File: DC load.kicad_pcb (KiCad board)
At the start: 2 copper layers, 33.3 x 44.4 mm, 23 parts, among them J1 CTL IN, J2 CTL OUT, J3 B+, J4 B-, Q1 IRFI540, U1 LM324

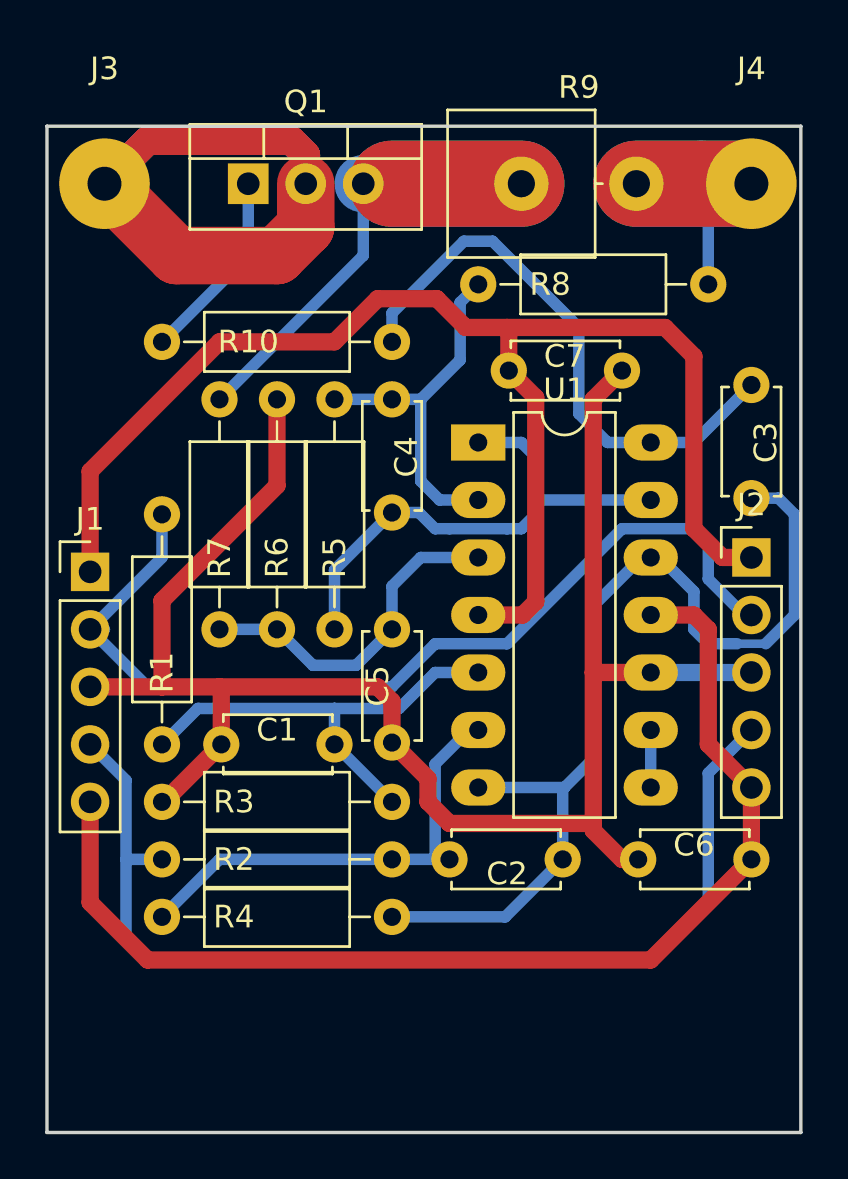
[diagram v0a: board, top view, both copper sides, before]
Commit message: Diagram: * Small offset so 0V is guaranteed to shut current off * Added zener to avoid high voltages and polarity reversal PCB: * Layout updated to new schematics
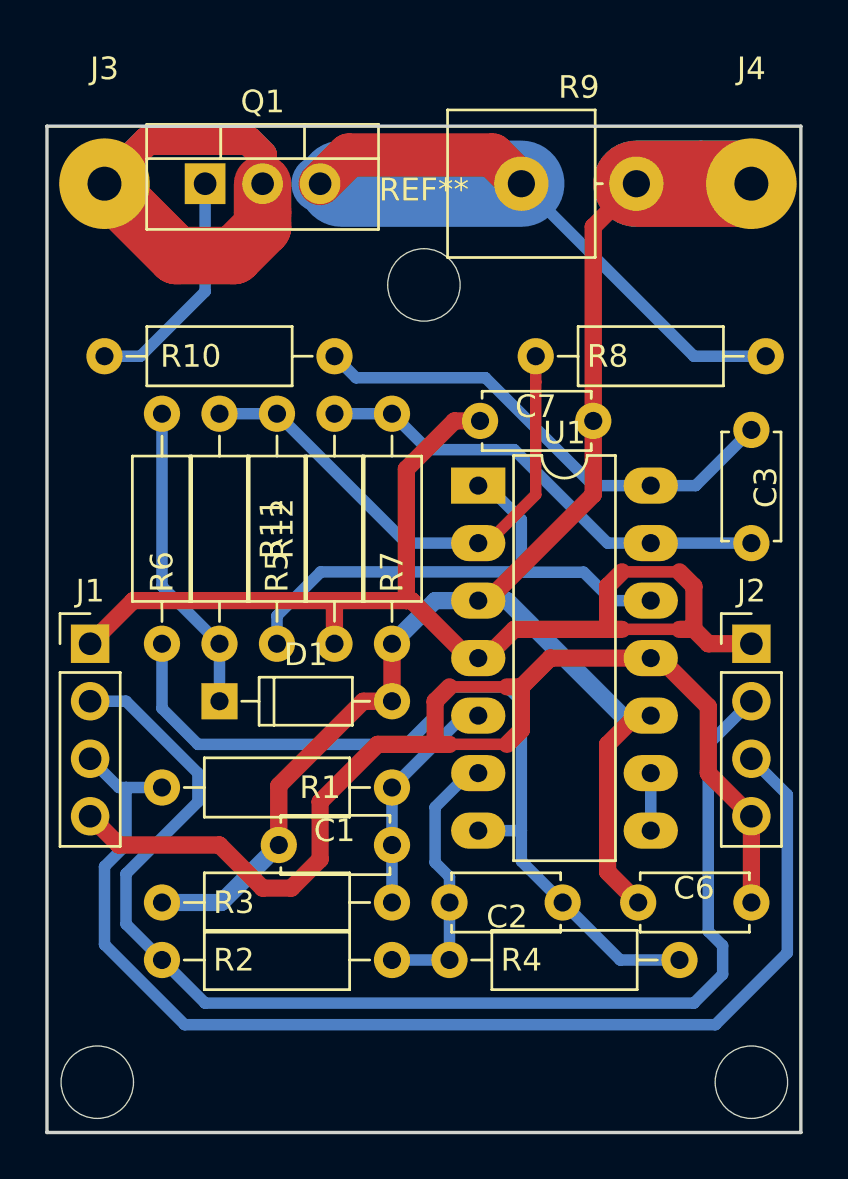
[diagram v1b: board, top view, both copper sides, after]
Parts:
- removed C4, C5: 1n, Capacitors_THT:C_Disc_D4.7mm_W2.5mm_P5.00mm
- added D1: 2v7, Diodes_THT:D_DO-35_SOD27_P7.62mm_Horizontal, F.Cu at (134.6, 120.7)
- added M1: MountingHole_3.2mm_M3, Mounting_Holes:MountingHole_3.2mm_M3, F.Cu at (129.2, 137.5)
- added M2: MountingHole_3.2mm_M3, Mounting_Holes:MountingHole_3.2mm_M3, F.Cu at (158.1, 137.5)
- added R11: 3k01, Resistors_THT:R_Axial_DIN0207_L6.3mm_D2.5mm_P10.16mm_Horizontal, F.Cu at (134.6, 108.0)
- added R12: 2M37, Resistors_THT:R_Axial_DIN0207_L6.3mm_D2.5mm_P10.16mm_Horizontal, F.Cu at (139.7, 118.1)
- added REF**: MountingHole_3.2mm_M3, Mounting_Holes:MountingHole_3.2mm_M3, F.Cu at (143.7, 102.3)
- C3: value 1n -> 10n
- J1, J2: footprint Pin_Headers:Pin_Header_Straight_1x05_Pitch2.54mm -> Pin_Headers:Pin_Header_Straight_1x04_Pitch2.54mm
- R3, R4: value 10k -> 5k11
- R5: value 13k3 -> 12k1
- R6: value 13k3 -> 3k01
- R7: value 1k -> 10k
- moved R4 12.8 mm to (154.9, 132.1)
- moved R1 10.3 mm to (142.2, 124.5), turned to 180 degrees
- moved R7 7.65 mm to (142.2, 108.0)
- moved C1 5.12 mm to (137.2, 127.0)
- moved R6 5.12 mm to (132.1, 118.1)
- moved R2 4.45 mm to (142.2, 132.1)
- moved R3 4.44 mm to (142.2, 129.5)
- moved R8 4.07 mm to (158.8, 105.4)
- moved J2 3.81 mm to (158.1, 118.1)
- moved J1 3.17 mm to (128.9, 118.1)
- moved R10 2.62 mm to (129.5, 105.4)
- moved R5 2.62 mm to (137.2, 108.0)
- moved C7 2.56 mm to (146.1, 108.3)
- moved C3 1.98 mm to (158.1, 108.7)
- moved U1 1.91 mm to (146.1, 111.1)
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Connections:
- C3 pad 2: Net-(C2-Pad1) -> Net-(C3-Pad2)
- J1 pad 3: GND -> Net-(J1-Pad3)
- J1 pad 4: Net-(J1-Pad4) -> VSS
- J2 pad 3: GND -> Net-(J1-Pad3)
- J2 pad 4: Net-(J1-Pad4) -> VSS
- J4 pad 1: Net-(J4-Pad1) -> GND
- R1 pad 2: Net-(J1-Pad2) -> Net-(J1-Pad3)
- R2 pad 2: Net-(J1-Pad4) -> Net-(J1-Pad2)
- R5 pad 2: Net-(C4-Pad2) -> Net-(R5-Pad2)
- R6 pad 1: Net-(C5-Pad1) -> Net-(C2-Pad1)
- R6 pad 2: GND -> Net-(D1-Pad1)
- R7 pad 1: Net-(Q1-Pad3) -> Net-(C3-Pad2)
- R7 pad 2: Net-(C5-Pad1) -> GND
- R8 pad 1: Net-(J4-Pad1) -> Net-(Q1-Pad3)
- R9 pad 2: Net-(J4-Pad1) -> GND
- U1 pad 1: Net-(C4-Pad2) -> Net-(R5-Pad2)
- U1 pad 12: Net-(C2-Pad1) -> Net-(R5-Pad2)
- U1 pad 13: Net-(C4-Pad2) -> Net-(C3-Pad2)
- U1 pad 3: Net-(C5-Pad1) -> GND
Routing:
- net Net-(J1-Pad3): track 0.00 -> 53.2 mm
- net Net-(J1-Pad4): track 46.4 -> 0.00 mm
- net Net-(R5-Pad2): track 0.00 -> 24.3 mm
- net Net-(C4-Pad2): track 23.5 -> 0.00 mm
- net Net-(C3-Pad2): track 0.00 -> 20.8 mm
- net Net-(C5-Pad1): track 15.2 -> 0.00 mm
- net Net-(J4-Pad1): track 14.7 -> 0.00 mm
- net Net-(D1-Pad1): track 0.00 -> 13.8 mm
- net Net-(J1-Pad2): track 42.7 -> 55.5 mm
- net Net-(C1-Pad2): track 20.5 -> 10.2 mm
- net VDD: track 61.4 -> 51.8 mm
- net Net-(Q1-Pad3): track 26.1 -> 35.0 mm
- net Net-(C2-Pad2): track 20.5 -> 12.1 mm
- net Net-(R11-Pad1): track 16.4 -> 23.3 mm
- net Net-(J3-Pad1): track 35.1 -> 29.3 mm
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
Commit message: Version 0.3: Reverted to more conventional opamp usage
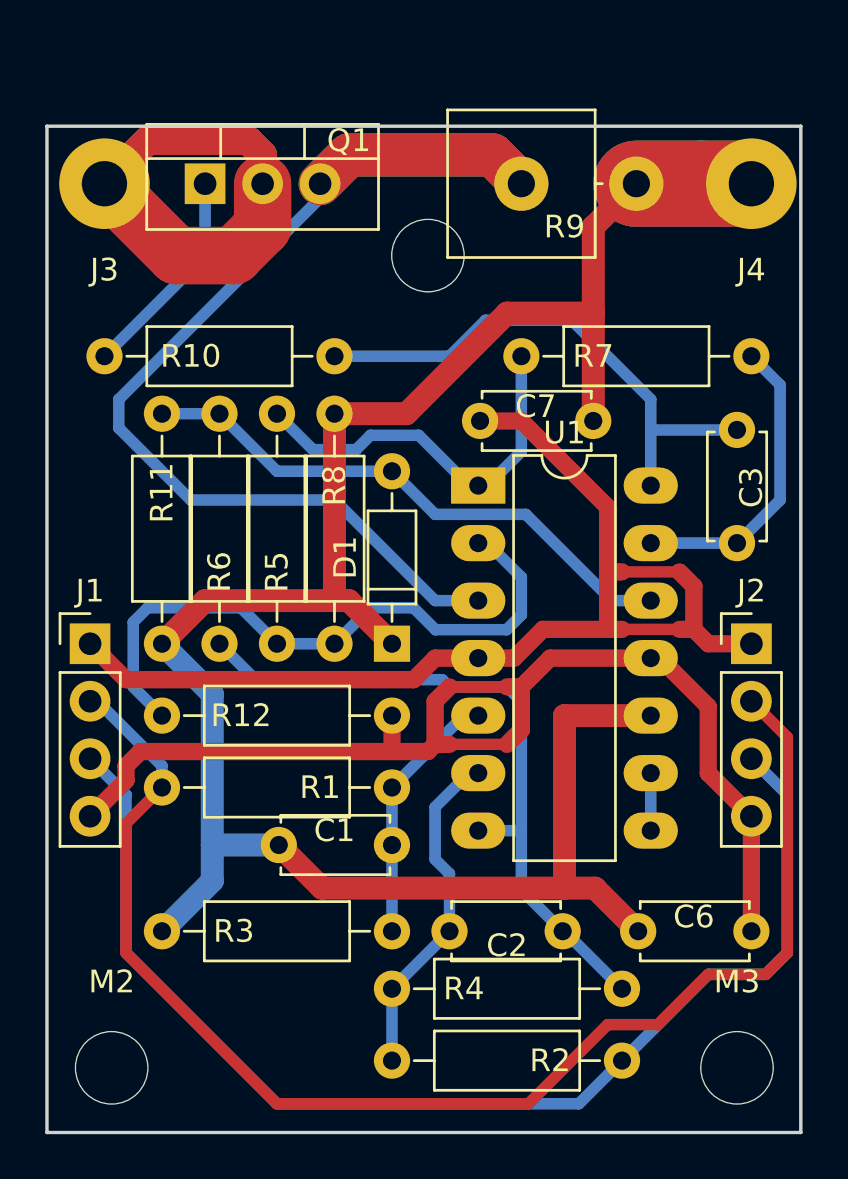
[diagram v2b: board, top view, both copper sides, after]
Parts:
- removed M1, REF**: MountingHole_3.2mm_M3, Mounting_Holes:MountingHole_3.2mm_M3
- added M3: 3.2mm, Mounting_Holes:MountingHole_3.2mm_M3_DIN965, F.Cu at (157.5, 136.8)
- added MP1: 3.2mm, Mounting_Holes:MountingHole_3.2mm_M3_DIN965, F.Cu at (143.8, 101.0)
- C3: value 10n -> 22n
- M2: value MountingHole_3.2mm_M3 -> 3.2mm; footprint Mounting_Holes:MountingHole_3.2mm_M3 -> Mounting_Holes:MountingHole_3.2mm_M3_DIN965
- R11, R6: value 3k01 -> 20k
- R12: value 2M37 -> 2M2
- R3, R4: value 5k11 -> 2k49
- R5: value 12k1 -> 2k
- moved M2 28.3 mm to (129.9, 136.8)
- moved R8 22.9 mm to (139.7, 118.1), turned to 90 degrees
- moved R7 16.1 mm to (158.1, 105.4), turned to 180 degrees
- moved R11 10.5 mm to (132.1, 118.1), turned to 90 degrees
- moved R12 8.25 mm to (132.1, 121.3), turned to 0 degrees
- moved D1 8.03 mm to (142.2, 118.1), turned to 90 degrees
- moved R2 4.44 mm to (142.2, 136.5), turned to 0 degrees
- moved R4 2.84 mm to (152.4, 133.3)
- moved R6 2.54 mm to (134.6, 118.1)
- moved C2 1.27 mm to (149.8, 130.8)
- moved C6 1.27 mm to (158.1, 130.8)
- moved R3 1.27 mm to (142.2, 130.8)
- moved C3 0.64 mm to (157.5, 108.7)
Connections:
- D1 pad 1: Net-(D1-Pad1) -> GND
- D1 pad 2: GND -> Net-(D1-Pad2)
- R1 pad 2: Net-(J1-Pad3) -> Net-(J1-Pad2)
- R11 pad 1: Net-(R11-Pad1) -> GND
- R11 pad 2: Net-(D1-Pad1) -> Net-(D1-Pad2)
- R12 pad 1: VDD -> Net-(R12-Pad1)
- R12 pad 2: Net-(C3-Pad2) -> VSS
- R2 pad 2: Net-(J1-Pad2) -> Net-(J1-Pad3)
- R5 pad 1: Net-(R11-Pad1) -> Net-(R5-Pad1)
- R5 pad 2: Net-(R5-Pad2) -> Net-(R12-Pad1)
- R6 pad 2: Net-(D1-Pad1) -> Net-(D1-Pad2)
- R7 pad 2: GND -> Net-(R5-Pad1)
- R8 pad 1: Net-(Q1-Pad3) -> Net-(R12-Pad1)
- R8 pad 2: Net-(R11-Pad1) -> GND
- U1 pad 1: Net-(R5-Pad2) -> Net-(R5-Pad1)
- U1 pad 12: Net-(R5-Pad2) -> Net-(D1-Pad2)
- U1 pad 2: Net-(R11-Pad1) -> Net-(R12-Pad1)
- U1 pad 3: GND -> Net-(Q1-Pad3)
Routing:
- net Net-(R12-Pad1): track 0.00 -> 28.6 mm
- net GND: track 74.4 -> 101.6 mm
- net Net-(D1-Pad2): track 0.00 -> 25.4 mm
- net Net-(R5-Pad2): track 24.3 -> 0.00 mm
- net Net-(R11-Pad1): track 23.3 -> 0.00 mm
- net Net-(Q1-Pad3): track 35.0 -> 53.8 mm
- net Net-(R5-Pad1): track 0.00 -> 17.5 mm
- net Net-(D1-Pad1): track 13.8 -> 0.00 mm
- net Net-(C2-Pad1): track 38.8 -> 30.9 mm
- net Net-(C3-Pad2): track 20.8 -> 13.4 mm
- net Net-(J1-Pad2): track 55.5 -> 59.8 mm
- net Net-(C2-Pad2): track 12.1 -> 15.0 mm
- net VDD: track 51.8 -> 49.6 mm
- net Net-(C3-Pad1): track 21.8 -> 23.7 mm
- net Net-(C1-Pad2): track 10.2 -> 11.5 mm
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
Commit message: Prepare for production
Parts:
- R9: footprint Resistors_THT:R_Axial_Power_L20.0mm_W6.4mm_P5.08mm_Vertical -> Capacitors_THT:C_Rect_L7.2mm_W4.5mm_P5.00mm_FKS2_FKP2_MKS2_MKP2
- moved D1 116.7 mm to (48.6, 48.6), turned to 270 degrees
- moved Q1 112.3 mm to (40.3, 35.9)
- moved R11 112.3 mm to (38.4, 56.2)
- moved R9 112.3 mm to (54.3, 35.9)
- moved B- 112.3 mm to (64.5, 35.9)
- moved C1 112.3 mm to (43.6, 65.1)
- moved C6 112.3 mm to (64.5, 68.9)
- moved J2 112.3 mm to (64.5, 56.2)
- moved R1 112.3 mm to (48.6, 62.5)
- moved R12 112.3 mm to (38.4, 59.4)
- moved R2 112.3 mm to (48.6, 74.6)
- moved R3 112.3 mm to (48.6, 68.9)
- moved R4 112.3 mm to (58.7, 71.4)
- moved R7 112.3 mm to (64.5, 43.5)
- moved U1 112.3 mm to (52.4, 49.2)
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- renumbered J3 to B+, J4 to B-, MP1 to M1
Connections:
- D1 pad 1: GND -> Net-(D1-Pad1)
- D1 pad 2: Net-(D1-Pad2) -> GND
- R11 pad 2: Net-(D1-Pad2) -> Net-(D1-Pad1)
- R6 pad 2: Net-(D1-Pad2) -> Net-(D1-Pad1)
- U1 pad 12: Net-(D1-Pad2) -> Net-(D1-Pad1)
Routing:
- net Net-(D1-Pad1): track 0.00 -> 25.4 mm
- net Net-(D1-Pad2): track 25.4 -> 0.00 mm
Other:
- board size 33.3 x 44.4 mm -> 100 x 88.9 mm
- board text added: "DC LOAD"
- board text added: "FEF 2019"
- board text added: "v1.0"

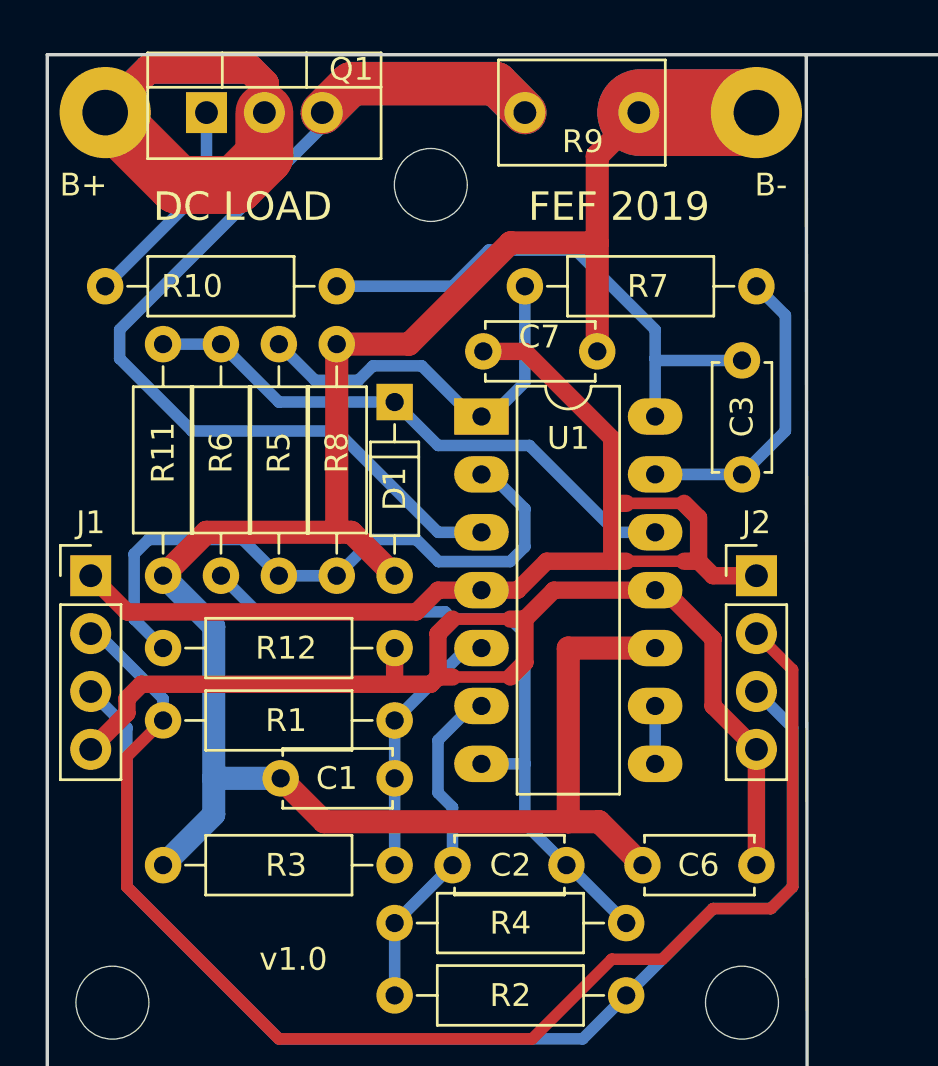
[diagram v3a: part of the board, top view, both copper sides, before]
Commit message: Changed overcurrent limiter
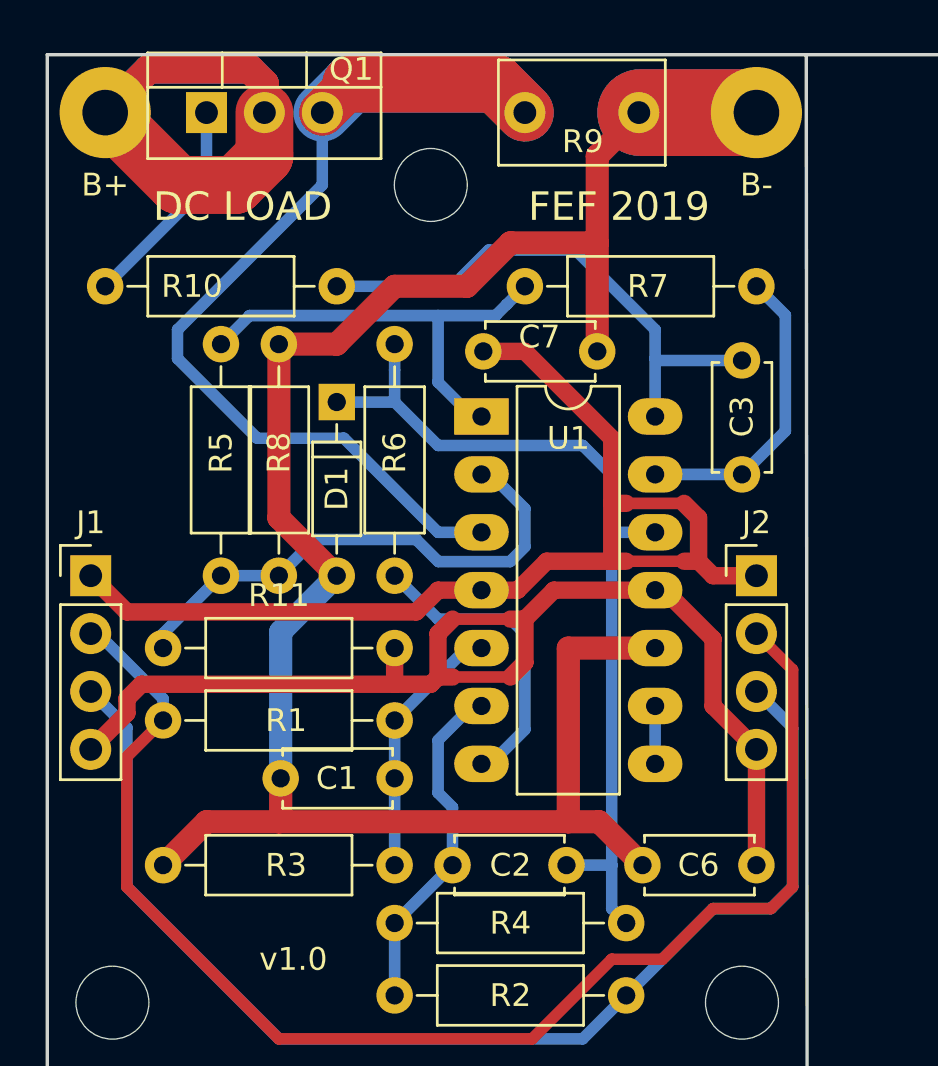
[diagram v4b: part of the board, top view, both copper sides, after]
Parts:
- removed R12: 2M2, Resistors_THT:R_Axial_DIN0207_L6.3mm_D2.5mm_P10.16mm_Horizontal
- D1: value 2v7 -> 3v0/5mA
- R11: value 20k -> 2M2
- R6: value 20k -> 1k4
- moved R6 7.62 mm to (48.6, 56.2)
- moved R11 3.18 mm to (38.4, 59.4), turned to 0 degrees
- moved D1 2.54 mm to (46.0, 48.6)
- moved R5 2.54 mm to (41.0, 46.0)
- moved R8 2.54 mm to (43.5, 56.2)
- renumbered B+ to J3, B- to J4
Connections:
- D1 pad 1: Net-(D1-Pad1) -> Net-(C2-Pad1)
- R11 pad 1: GND -> Net-(R11-Pad1)
- R11 pad 2: Net-(D1-Pad1) -> VSS
- R5 pad 2: Net-(R12-Pad1) -> Net-(R11-Pad1)
- R6 pad 1: Net-(C2-Pad1) -> Net-(R6-Pad1)
- R6 pad 2: Net-(D1-Pad1) -> Net-(C2-Pad1)
- R8 pad 1: Net-(R12-Pad1) -> Net-(R11-Pad1)
- U1 pad 12: Net-(D1-Pad1) -> Net-(C2-Pad1)
- U1 pad 2: Net-(R12-Pad1) -> Net-(R11-Pad1)
- U1 pad 7: Net-(C2-Pad1) -> Net-(R6-Pad1)
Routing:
- net Net-(R12-Pad1): track 28.6 -> 0.00 mm
- net Net-(D1-Pad1): track 25.4 -> 0.00 mm
- net Net-(R11-Pad1): track 0.00 -> 23.5 mm
- net Net-(R6-Pad1): track 0.00 -> 13.5 mm
- net Net-(C2-Pad1): track 30.9 -> 40.2 mm
- net GND: track 101.6 -> 94.9 mm
- net Net-(Q1-Pad3): track 53.8 -> 50.2 mm
- net Net-(R5-Pad1): track 17.5 -> 20.2 mm
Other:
- board text added: "B+"
- board text added: "B-"
